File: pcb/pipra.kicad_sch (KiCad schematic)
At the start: 200 parts, among them J1 HRO_TYPE-C-31-M-14, J2 SWD, J3 Battery, J4 HRO_TYPE-C-31-M-14, J5 SWD, J6 Battery, Q1 2N7002, Q2 2N7002, SW1 RST, SW10 EC_SW, SW11 EC_SW, SW12 EC_SW, SW13 EC_SW, SW14 EC_SW, SW15 EC_SW, SW16 EC_SW, SW17 EC_SW, SW18 RotaryEncoder_Switch, SW19 RST, SW2 PWR, SW20 PWR, SW21 EC_SW, SW22 EC_SW, SW23 EC_SW, SW24 EC_SW, SW25 EC_SW, SW26 EC_SW, SW27 EC_SW, SW28 EC_SW, SW29 EC_SW, SW3 EC_SW, SW30 EC_SW, SW31 EC_SW, SW32 EC_SW, SW33 EC_SW, SW34 EC_SW, SW35 EC_SW, SW36 RotaryEncoder_Switch, SW4 EC_SW, SW5 EC_SW, SW6 EC_SW, SW7 EC_SW, SW8 EC_SW, SW9 EC_SW, U1 SRV05-4, U10 MAX17048, U11 74HC4051, U12 OPA320SxDBV, U2 nRF52840_E73-2G4M08S1C, U3 BQ24075, U4 MAX17048, U5 74HC4051, U6 OPA320SxDBV, U7 SRV05-4, U8 nRF52840_E73-2G4M08S1C, U9 BQ24075, Y1 32.768 KHz, Y2 32.768 KHz

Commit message: Update production files
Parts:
- D2, D3, D4, D6, D7, D8: now not fitted; now left out of the parts list
- J1, J4: FT Position Offset (none) -> 0,1.4605
- JP1, JP2, R54: now left out of the parts list
- SW10, SW11, SW12, SW13, SW14, SW15, SW16, SW17, SW21, SW22, SW23, SW24, SW25, SW26, SW27, SW28, SW29, SW3, SW30, SW31, SW32, SW33, SW34, SW35, SW4, SW5, SW6, SW7, SW8, SW9: footprint ssbb_parts:EC_Pad_L84 -> ssbb_parts:EC_Pad_L84_18x16; symbol pipra:EC_SW -> ssbb_parts:EC_SW; now left out of the parts list
- U1, U12, U6, U7: FT Rotation Offset (none) -> 90
- U2, U8: FT Position Offset (none) -> 0,-1.9685; FT Rotation Offset (none) -> 180

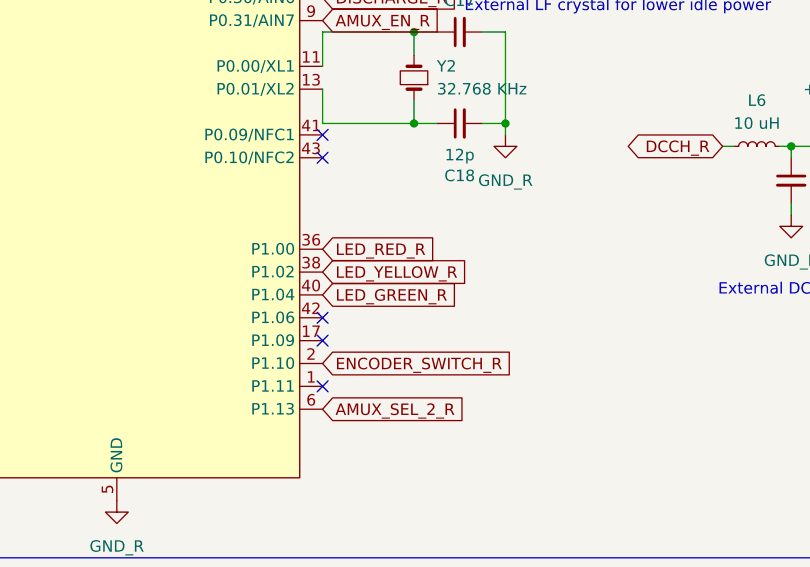
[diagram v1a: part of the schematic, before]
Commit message: Unify led pins
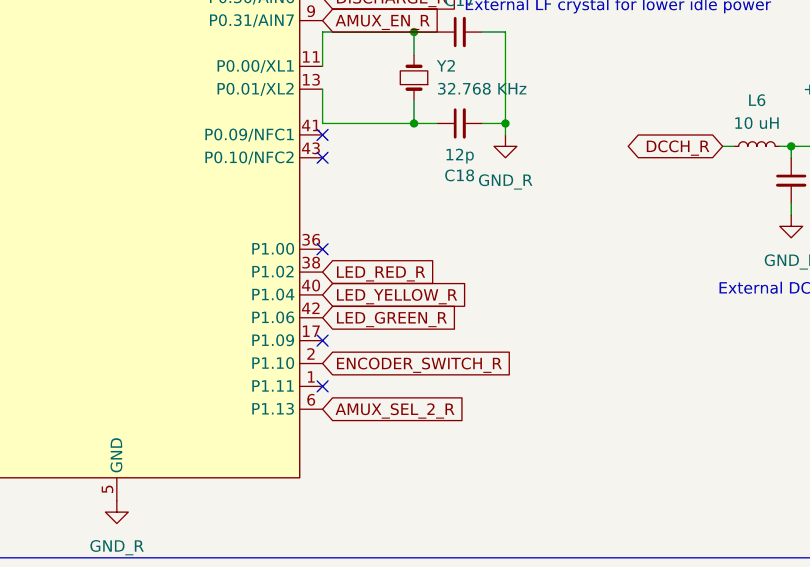
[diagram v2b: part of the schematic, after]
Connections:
- net LED_GREEN_R: now also U8.42 (P1.06); no longer U8.40 (P1.04)
- net LED_RED_R: now also U8.38 (P1.02); no longer U8.36 (P1.00)
- net LED_YELLOW_R: now also U8.40 (P1.04); no longer U8.38 (P1.02)
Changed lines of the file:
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@@
 	)
 	(no_connect
+		(at 548.64 81.28)
+	)
+	(no_connect
 		(at 144.78 60.96)
 	)
@@
 	)
 	(no_connect
-		(at 548.64 88.9)
-	)
-	(no_connect
 		(at 173.99 96.52)
 	)
@@
 	(global_label "LED_YELLOW_R"
 		(shape input)
-		(at 548.64 83.82 0)
+		(at 548.64 86.36 0)
 		(fields_autoplaced yes)
 		(effects
@@
 		)
 		(property "Intersheetrefs" "${INTERSHEET_REFS}"
-			(at 565.3532 83.82 0)
+			(at 565.3532 86.36 0)
 			(effects
 				(font
@@
 		)
 	)
-	(global_label "LED_GREEN_R"
-		(shape input)
-		(at 548.64 86.36 0)
-		(fields_autoplaced yes)
-		(effects
-			(font
-				(size 1.27 1.27)
-			)
-			(justify left)
-		)
-		(property "Intersheetrefs" "${INTERSHEET_REFS}"
-			(at 564.446 86.36 0)
-			(effects
-				(font
-					(size 1.27 1.27)
-				)
-				(justify left)
-				(hide yes)
-			)
-		)
-	)
 	(global_label "ENCODER_SWITCH"
 		(shape input)
@@
 		)
 	)
+	(global_label "LED_GREEN_R"
+		(shape input)
+		(at 548.64 88.9 0)
+		(fields_autoplaced yes)
+		(effects
+			(font
+				(size 1.27 1.27)
+			)
+			(justify left)
+		)
+		(property "Intersheetrefs" "${INTERSHEET_REFS}"
+			(at 564.446 88.9 0)
+			(effects
+				(font
+					(size 1.27 1.27)
+				)
+				(justify left)
+				(hide yes)
+			)
+		)
+	)
 	(global_label "AMUX_SEL_1_R"
 		(shape input)
@@
 	(global_label "LED_RED_R"
 		(shape input)
-		(at 548.64 81.28 0)
+		(at 548.64 83.82 0)
 		(fields_autoplaced yes)
 		(effects
@@
 		)
 		(property "Intersheetrefs" "${INTERSHEET_REFS}"
-			(at 561.9665 81.28 0)
+			(at 561.9665 83.82 0)
 			(effects
 				(font
